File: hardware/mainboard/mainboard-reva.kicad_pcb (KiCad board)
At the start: 4 copper layers, 88 x 48 mm, 77 parts, among them J1 USB-C, J2 BATTERY, J3 SM05B-GHS-TB / ENCODER, J4 SM03B-GHS-TB / SNOOZE, J5 Molex 54550-2472 / GDEY037T03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, J6 Molex 54550-0672 / FL21 front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, J7 SPEAKER, J8 SM02B-GHS-TB / WAKE_LED, Q2 AO3400A / WAKE, U1 ESP32-S3-WROOM-1-N8, U2 BQ24074RGTR, U3 TPS62840DLCR, U4 RV-3028-C7, U5 VEML7700, U6 MAX98357AETE+T, U7 USBLC6-2SC6

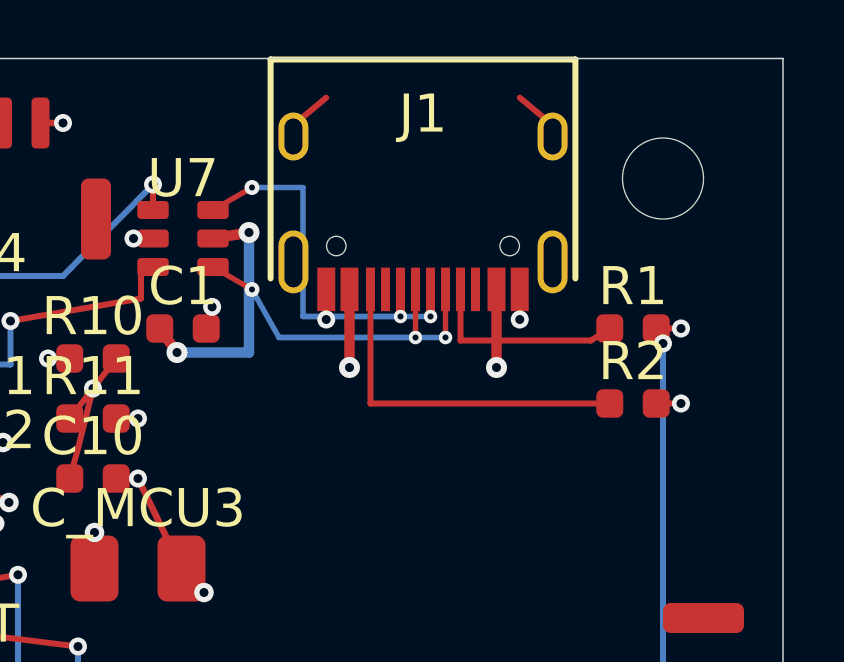
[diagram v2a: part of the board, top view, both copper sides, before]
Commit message: fix(mainboard): rebuild USB-C breakout with rule-compliant geometry
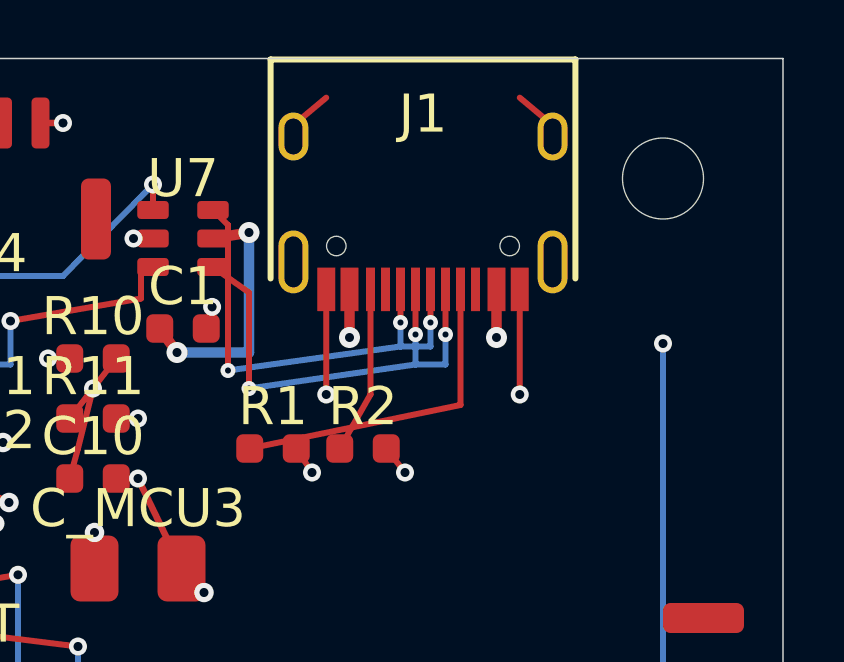
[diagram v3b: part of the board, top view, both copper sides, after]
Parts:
- moved R1 12.6 mm to (71.0, 13.0)
- moved R2 9.12 mm to (74.0, 13.0)
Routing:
- net USB_CC2: track 11.8 -> 5.58 mm
- net GND: track 104.1 -> 109.5 mm
- net USB_CC1: track 6.80 -> 11.0 mm
- net VBUS_USB: track 94.0 -> 91.2 mm
- net USB_D+_CONN: track 16.8 -> 16.2 mm
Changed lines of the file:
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@@
     (pad "" np_thru_hole circle (at -2.89 -2.60) (size 0.65 0.65) (drill 0.65) (layers "*.Cu" "*.Mask"))
     (pad "" np_thru_hole circle (at 2.89 -2.60) (size 0.65 0.65) (drill 0.65) (layers "*.Cu" "*.Mask"))
-    (pad "A1" smd rect (at -3.225 -4.045) (size 0.6 1.45) (layers "F.Cu" "F.Paste" "F.Mask") (net 1 "GND"))
-    (pad "A4" smd rect (at -2.45 -4.045) (size 0.6 1.45) (layers "F.Cu" "F.Paste" "F.Mask") (net 2 "VBUS_USB"))
+    (pad "A1" smd rect (at -3.225 -4.045) (size 0.6 1.45) (layers "F.Cu" "F.Paste" "F.Mask") (clearance 0.15) (net 1 "GND"))
+    (pad "A4" smd rect (at -2.45 -4.045) (size 0.6 1.45) (layers "F.Cu" "F.Paste" "F.Mask") (clearance 0.15) (net 2 "VBUS_USB"))
     (pad "A5" smd rect (at -1.25 -4.045) (size 0.3 1.45) (layers "F.Cu" "F.Paste" "F.Mask") (net 21 "USB_CC1"))
     (pad "A6" smd rect (at -0.25 -4.045) (size 0.3 1.45) (layers "F.Cu" "F.Paste" "F.Mask") (net 59 "USB_D+_CONN"))
     (pad "A7" smd rect (at 0.25 -4.045) (size 0.3 1.45) (layers "F.Cu" "F.Paste" "F.Mask") (net 60 "USB_D-_CONN"))
     (pad "A8" smd rect (at 1.25 -4.045) (size 0.3 1.45) (layers "F.Cu" "F.Paste" "F.Mask"))
-    (pad "A9" smd rect (at 2.45 -4.045) (size 0.6 1.45) (layers "F.Cu" "F.Paste" "F.Mask") (net 2 "VBUS_USB"))
-    (pad "A12" smd rect (at 3.225 -4.045) (size 0.6 1.45) (layers "F.Cu" "F.Paste" "F.Mask") (net 1 "GND"))
+    (pad "A9" smd rect (at 2.45 -4.045) (size 0.6 1.45) (layers "F.Cu" "F.Paste" "F.Mask") (clearance 0.15) (net 2 "VBUS_USB"))
+    (pad "A12" smd rect (at 3.225 -4.045) (size 0.6 1.45) (layers "F.Cu" "F.Paste" "F.Mask") (clearance 0.15) (net 1 "GND"))
     (pad "B5" smd rect (at 1.75 -4.045) (size 0.3 1.45) (layers "F.Cu" "F.Paste" "F.Mask") (net 22 "USB_CC2"))
     (pad "B6" smd rect (at 0.75 -4.045) (size 0.3 1.45) (layers "F.Cu" "F.Paste" "F.Mask") (net 59 "USB_D+_CONN"))
@@
     (pad "6" smd roundrect (at 1 -0.95) (size 1.05 0.6) (layers "F.Cu" "F.Paste" "F.Mask") (roundrect_rratio 0.2) (net 59 "USB_D+_CONN"))
   )
-  (footprint "Resistor_SMD:R_0603_1608Metric" (layer "F.Cu") (at 83.0 9.0)
+  (footprint "Resistor_SMD:R_0603_1608Metric" (layer "F.Cu") (at 71.0 13.0)
     (property "Reference" "R1" (at 0 -1.4) (layer "F.SilkS"))
     (property "Value" "5.1k CC1" (at 0 1.4) (layer "F.Fab") hide)
@@
     (pad "2" smd roundrect (at 0.775 0) (size 0.9 0.95) (layers "F.Cu" "F.Paste" "F.Mask") (roundrect_rratio 0.25) (net 1 "GND"))
   )
-  (footprint "Resistor_SMD:R_0603_1608Metric" (layer "F.Cu") (at 83.0 11.5)
+  (footprint "Resistor_SMD:R_0603_1608Metric" (layer "F.Cu") (at 74.0 13.0)
     (property "Reference" "R2" (at 0 -1.4) (layer "F.SilkS"))
     (property "Value" "5.1k CC2" (at 0 1.4) (layer "F.Fab") hide)
@@
   (via (at 73.0 40.8) (size 0.60) (drill 0.30) (layers "F.Cu" "B.Cu") (net 42))
   (segment (start 73.0 40.8) (end 73.0 42.0) (width 0.30) (layer "F.Cu") (net 42))
-  (segment (start 72.775 7.695) (end 72.775 8.70) (width 0.20) (layer "F.Cu") (net 1))
-  (via (at 72.775 8.70) (size 0.60) (drill 0.30) (layers "F.Cu" "B.Cu") (net 1))
-  (segment (start 79.225 7.695) (end 79.225 8.70) (width 0.20) (layer "F.Cu") (net 1))
-  (via (at 79.225 8.70) (size 0.60) (drill 0.30) (layers "F.Cu" "B.Cu") (net 1))
-  (segment (start 83.775 9.0) (end 84.6 9.0) (width 0.20) (layer "F.Cu") (net 1))
-  (via (at 84.6 9.0) (size 0.60) (drill 0.30) (layers "F.Cu" "B.Cu") (net 1))
-  (segment (start 83.775 11.5) (end 84.6 11.5) (width 0.20) (layer "F.Cu") (net 1))
-  (via (at 84.6 11.5) (size 0.60) (drill 0.30) (layers "F.Cu" "B.Cu") (net 1))
-  (segment (start 77.25 7.695) (end 77.25 9.40) (width 0.20) (layer "F.Cu") (net 21))
-  (segment (start 77.25 9.40) (end 81.60 9.40) (width 0.20) (layer "F.Cu") (net 21))
-  (segment (start 81.60 9.40) (end 82.225 9.00) (width 0.20) (layer "F.Cu") (net 21))
-  (segment (start 74.25 7.695) (end 74.25 11.50) (width 0.20) (layer "F.Cu") (net 22))
-  (segment (start 74.25 11.50) (end 82.225 11.50) (width 0.20) (layer "F.Cu") (net 22))
-  (segment (start 75.25 7.695) (end 75.25 8.60) (width 0.18) (layer "F.Cu") (net 59))
-  (via (at 75.25 8.60) (size 0.45) (drill 0.20) (layers "F.Cu" "B.Cu") (net 59))
-  (segment (start 76.25 7.695) (end 76.25 8.60) (width 0.18) (layer "F.Cu") (net 59))
-  (via (at 76.25 8.60) (size 0.45) (drill 0.20) (layers "F.Cu" "B.Cu") (net 59))
-  (segment (start 75.25 8.60) (end 72.00 8.60) (width 0.18) (layer "B.Cu") (net 59))
-  (segment (start 76.25 8.60) (end 72.00 8.60) (width 0.18) (layer "B.Cu") (net 59))
-  (segment (start 72.00 8.60) (end 72.00 4.30) (width 0.18) (layer "B.Cu") (net 59))
-  (segment (start 72.00 4.30) (end 70.30 4.30) (width 0.18) (layer "B.Cu") (net 59))
-  (via (at 70.30 4.30) (size 0.50) (drill 0.20) (layers "F.Cu" "B.Cu") (net 59))
-  (segment (start 70.30 4.30) (end 69.0 5.05) (width 0.18) (layer "F.Cu") (net 59))
-  (segment (start 75.75 7.695) (end 75.75 9.30) (width 0.18) (layer "F.Cu") (net 60))
-  (via (at 75.75 9.30) (size 0.45) (drill 0.20) (layers "F.Cu" "B.Cu") (net 60))
-  (segment (start 76.75 7.695) (end 76.75 9.30) (width 0.18) (layer "F.Cu") (net 60))
-  (via (at 76.75 9.30) (size 0.45) (drill 0.20) (layers "F.Cu" "B.Cu") (net 60))
-  (segment (start 75.75 9.30) (end 71.20 9.30) (width 0.18) (layer "B.Cu") (net 60))
-  (segment (start 76.75 9.30) (end 71.20 9.30) (width 0.18) (layer "B.Cu") (net 60))
-  (segment (start 71.20 9.30) (end 70.30 7.70) (width 0.18) (layer "B.Cu") (net 60))
-  (via (at 70.30 7.70) (size 0.50) (drill 0.20) (layers "F.Cu" "B.Cu") (net 60))
-  (segment (start 70.30 7.70) (end 69.0 6.95) (width 0.18) (layer "F.Cu") (net 60))
-  (segment (start 73.55 7.695) (end 73.55 10.30) (width 0.35) (layer "F.Cu") (net 2))
-  (via (at 73.55 10.30) (size 0.70) (drill 0.30) (layers "F.Cu" "B.Cu") (net 2))
-  (segment (start 78.45 7.695) (end 78.45 10.30) (width 0.35) (layer "F.Cu") (net 2))
-  (via (at 78.45 10.30) (size 0.70) (drill 0.30) (layers "F.Cu" "B.Cu") (net 2))
-  (segment (start 78.45 10.30) (end 73.55 10.30) (width 0.50) (layer "In2.Cu") (net 2))
-  (segment (start 73.55 10.30) (end 69.80 4.60) (width 0.50) (layer "In2.Cu") (net 2))
+  (segment (start 72.775 7.695) (end 72.775 11.20) (width 0.20) (layer "F.Cu") (net 1))
+  (via (at 72.775 11.20) (size 0.60) (drill 0.30) (layers "F.Cu" "B.Cu") (net 1))
+  (segment (start 79.225 7.695) (end 79.225 11.20) (width 0.20) (layer "F.Cu") (net 1))
+  (via (at 79.225 11.20) (size 0.60) (drill 0.30) (layers "F.Cu" "B.Cu") (net 1))
+  (segment (start 77.25 7.695) (end 77.25 11.55) (width 0.20) (layer "F.Cu") (net 21))
+  (segment (start 77.25 11.55) (end 70.225 13.00) (width 0.20) (layer "F.Cu") (net 21))
+  (segment (start 71.775 13.00) (end 72.30 13.80) (width 0.20) (layer "F.Cu") (net 1))
+  (via (at 72.30 13.80) (size 0.60) (drill 0.30) (layers "F.Cu" "B.Cu") (net 1))
+  (segment (start 74.25 7.695) (end 74.25 11.20) (width 0.20) (layer "F.Cu") (net 22))
+  (segment (start 74.25 11.20) (end 73.225 13.00) (width 0.20) (layer "F.Cu") (net 22))
+  (segment (start 74.775 13.00) (end 75.40 13.80) (width 0.20) (layer "F.Cu") (net 1))
+  (via (at 75.40 13.80) (size 0.60) (drill 0.30) (layers "F.Cu" "B.Cu") (net 1))
+  (segment (start 75.25 7.695) (end 75.25 8.80) (width 0.20) (layer "F.Cu") (net 59))
+  (via (at 75.25 8.80) (size 0.50) (drill 0.20) (layers "F.Cu" "B.Cu") (net 59))
+  (segment (start 76.25 7.695) (end 76.25 8.80) (width 0.20) (layer "F.Cu") (net 59))
+  (via (at 76.25 8.80) (size 0.50) (drill 0.20) (layers "F.Cu" "B.Cu") (net 59))
+  (segment (start 75.25 8.80) (end 75.25 9.60) (width 0.20) (layer "B.Cu") (net 59))
+  (segment (start 76.25 8.80) (end 76.25 9.60) (width 0.20) (layer "B.Cu") (net 59))
+  (segment (start 76.25 9.60) (end 75.25 9.60) (width 0.20) (layer "B.Cu") (net 59))
+  (segment (start 75.25 9.60) (end 69.50 10.40) (width 0.20) (layer "B.Cu") (net 59))
+  (via (at 69.50 10.40) (size 0.50) (drill 0.20) (layers "F.Cu" "B.Cu") (net 59))
+  (segment (start 69.50 10.40) (end 69.50 5.55) (width 0.20) (layer "F.Cu") (net 59))
+  (segment (start 69.50 5.55) (end 69.0 5.05) (width 0.20) (layer "F.Cu") (net 59))
+  (segment (start 75.75 7.695) (end 75.75 9.20) (width 0.20) (layer "F.Cu") (net 60))
+  (via (at 75.75 9.20) (size 0.50) (drill 0.20) (layers "F.Cu" "B.Cu") (net 60))
+  (segment (start 76.75 7.695) (end 76.75 9.20) (width 0.20) (layer "F.Cu") (net 60))
+  (via (at 76.75 9.20) (size 0.50) (drill 0.20) (layers "F.Cu" "B.Cu") (net 60))
+  (segment (start 75.75 9.20) (end 75.75 10.20) (width 0.20) (layer "B.Cu") (net 60))
+  (segment (start 76.75 9.20) (end 76.75 10.20) (width 0.20) (layer "B.Cu") (net 60))
+  (segment (start 76.75 10.20) (end 75.75 10.20) (width 0.20) (layer "B.Cu") (net 60))
+  (segment (start 75.75 10.20) (end 70.20 11.00) (width 0.20) (layer "B.Cu") (net 60))
+  (via (at 70.20 11.00) (size 0.50) (drill 0.20) (layers "F.Cu" "B.Cu") (net 60))
+  (segment (start 70.20 11.00) (end 70.20 7.80) (width 0.20) (layer "F.Cu") (net 60))
+  (segment (start 70.20 7.80) (end 69.0 6.95) (width 0.20) (layer "F.Cu") (net 60))
+  (segment (start 73.55 7.695) (end 73.55 9.30) (width 0.35) (layer "F.Cu") (net 2))
+  (via (at 73.55 9.30) (size 0.70) (drill 0.30) (layers "F.Cu" "B.Cu") (net 2))
+  (segment (start 78.45 7.695) (end 78.45 9.30) (width 0.35) (layer "F.Cu") (net 2))
+  (via (at 78.45 9.30) (size 0.70) (drill 0.30) (layers "F.Cu" "B.Cu") (net 2))
+  (segment (start 78.45 9.30) (end 73.55 9.30) (width 0.50) (layer "In2.Cu") (net 2))
+  (segment (start 73.55 9.30) (end 69.80 4.60) (width 0.50) (layer "In2.Cu") (net 2))
   (segment (start 69.0 6.0) (end 70.20 5.80) (width 0.35) (layer "F.Cu") (net 2))
   (via (at 70.20 5.80) (size 0.70) (drill 0.30) (layers "F.Cu" "B.Cu") (net 2))

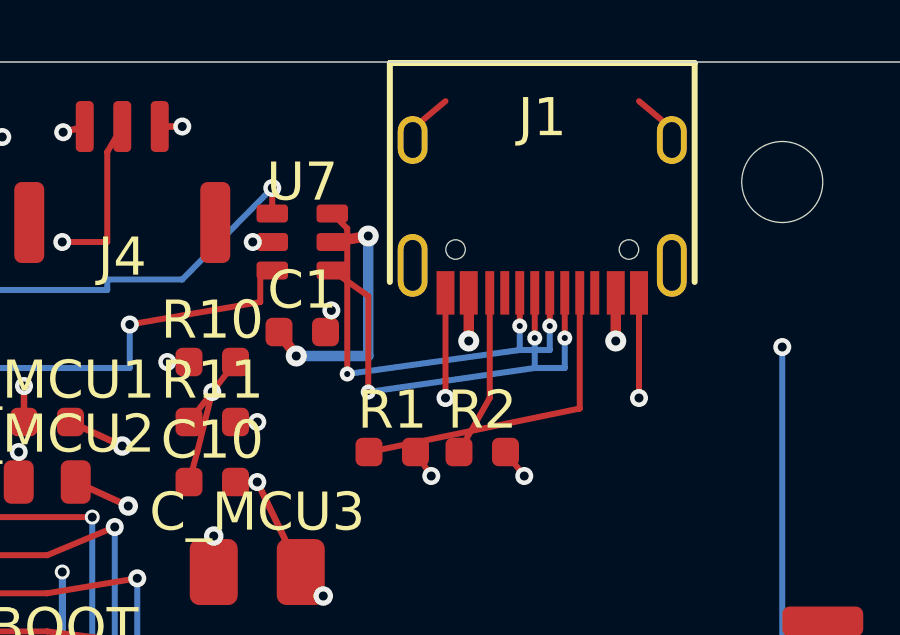
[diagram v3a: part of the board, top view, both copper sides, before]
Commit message: fix(mainboard): separate USB data layers and avoid shell crossing
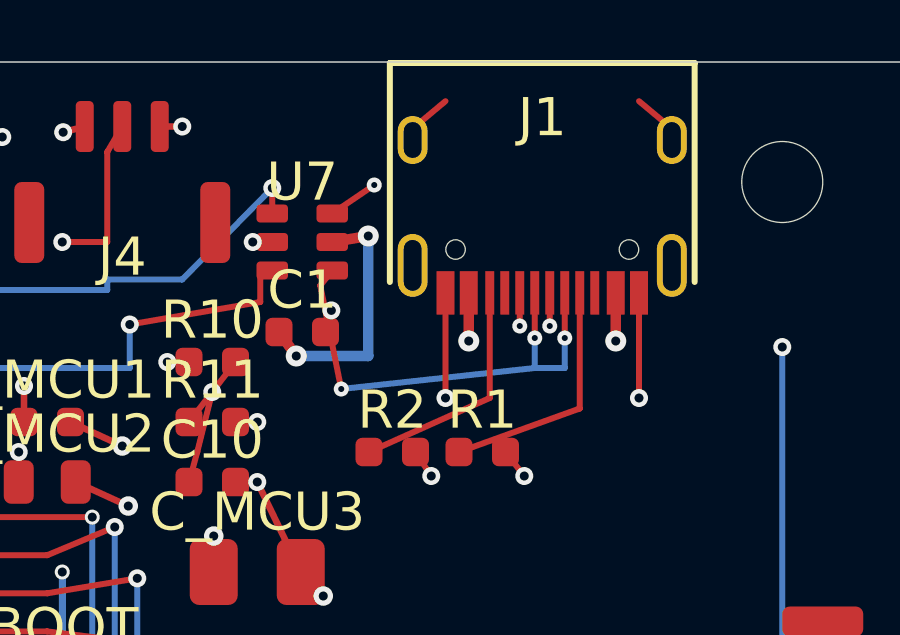
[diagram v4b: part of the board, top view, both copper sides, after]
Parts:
- moved R1 3.00 mm to (74.0, 13.0)
- moved R2 3.00 mm to (71.0, 13.0)
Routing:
- net VBUS_USB: track 91.2 -> 97.4 mm
- net USB_CC1: track 11.0 -> 8.13 mm
- net USB_CC2: track 5.58 -> 7.91 mm
- net USB_D+_CONN: track 16.2 -> 13.8 mm
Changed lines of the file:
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@@
     (pad "6" smd roundrect (at 1 -0.95) (size 1.05 0.6) (layers "F.Cu" "F.Paste" "F.Mask") (roundrect_rratio 0.2) (net 59 "USB_D+_CONN"))
   )
-  (footprint "Resistor_SMD:R_0603_1608Metric" (layer "F.Cu") (at 71.0 13.0)
+  (footprint "Resistor_SMD:R_0603_1608Metric" (layer "F.Cu") (at 74.0 13.0)
     (property "Reference" "R1" (at 0 -1.4) (layer "F.SilkS"))
     (property "Value" "5.1k CC1" (at 0 1.4) (layer "F.Fab") hide)
@@
     (pad "2" smd roundrect (at 0.775 0) (size 0.9 0.95) (layers "F.Cu" "F.Paste" "F.Mask") (roundrect_rratio 0.25) (net 1 "GND"))
   )
-  (footprint "Resistor_SMD:R_0603_1608Metric" (layer "F.Cu") (at 74.0 13.0)
+  (footprint "Resistor_SMD:R_0603_1608Metric" (layer "F.Cu") (at 71.0 13.0)
     (property "Reference" "R2" (at 0 -1.4) (layer "F.SilkS"))
     (property "Value" "5.1k CC2" (at 0 1.4) (layer "F.Fab") hide)
@@
   (via (at 79.225 11.20) (size 0.60) (drill 0.30) (layers "F.Cu" "B.Cu") (net 1))
   (segment (start 77.25 7.695) (end 77.25 11.55) (width 0.20) (layer "F.Cu") (net 21))
-  (segment (start 77.25 11.55) (end 70.225 13.00) (width 0.20) (layer "F.Cu") (net 21))
+  (segment (start 77.25 11.55) (end 73.225 13.00) (width 0.20) (layer "F.Cu") (net 21))
   (segment (start 71.775 13.00) (end 72.30 13.80) (width 0.20) (layer "F.Cu") (net 1))
   (via (at 72.30 13.80) (size 0.60) (drill 0.30) (layers "F.Cu" "B.Cu") (net 1))
   (segment (start 74.25 7.695) (end 74.25 11.20) (width 0.20) (layer "F.Cu") (net 22))
-  (segment (start 74.25 11.20) (end 73.225 13.00) (width 0.20) (layer "F.Cu") (net 22))
+  (segment (start 74.25 11.20) (end 70.225 13.00) (width 0.20) (layer "F.Cu") (net 22))
   (segment (start 74.775 13.00) (end 75.40 13.80) (width 0.20) (layer "F.Cu") (net 1))
   (via (at 75.40 13.80) (size 0.60) (drill 0.30) (layers "F.Cu" "B.Cu") (net 1))
@@
   (segment (start 76.25 7.695) (end 76.25 8.80) (width 0.20) (layer "F.Cu") (net 59))
   (via (at 76.25 8.80) (size 0.50) (drill 0.20) (layers "F.Cu" "B.Cu") (net 59))
-  (segment (start 75.25 8.80) (end 75.25 9.60) (width 0.20) (layer "B.Cu") (net 59))
-  (segment (start 76.25 8.80) (end 76.25 9.60) (width 0.20) (layer "B.Cu") (net 59))
-  (segment (start 76.25 9.60) (end 75.25 9.60) (width 0.20) (layer "B.Cu") (net 59))
-  (segment (start 75.25 9.60) (end 69.50 10.40) (width 0.20) (layer "B.Cu") (net 59))
-  (via (at 69.50 10.40) (size 0.50) (drill 0.20) (layers "F.Cu" "B.Cu") (net 59))
-  (segment (start 69.50 10.40) (end 69.50 5.55) (width 0.20) (layer "F.Cu") (net 59))
-  (segment (start 69.50 5.55) (end 69.0 5.05) (width 0.20) (layer "F.Cu") (net 59))
+  (segment (start 75.25 8.80) (end 75.25 9.60) (width 0.20) (layer "In1.Cu") (net 59))
+  (segment (start 76.25 8.80) (end 76.25 9.60) (width 0.20) (layer "In1.Cu") (net 59))
+  (segment (start 76.25 9.60) (end 75.25 9.60) (width 0.20) (layer "In1.Cu") (net 59))
+  (segment (start 75.25 9.60) (end 70.40 4.10) (width 0.20) (layer "In1.Cu") (net 59))
+  (via (at 70.40 4.10) (size 0.50) (drill 0.20) (layers "F.Cu" "B.Cu") (net 59))
+  (segment (start 70.40 4.10) (end 69.0 5.05) (width 0.20) (layer "F.Cu") (net 59))
   (segment (start 75.75 7.695) (end 75.75 9.20) (width 0.20) (layer "F.Cu") (net 60))
   (via (at 75.75 9.20) (size 0.50) (drill 0.20) (layers "F.Cu" "B.Cu") (net 60))
@@
   (segment (start 76.75 9.20) (end 76.75 10.20) (width 0.20) (layer "B.Cu") (net 60))
   (segment (start 76.75 10.20) (end 75.75 10.20) (width 0.20) (layer "B.Cu") (net 60))
-  (segment (start 75.75 10.20) (end 70.20 11.00) (width 0.20) (layer "B.Cu") (net 60))
-  (via (at 70.20 11.00) (size 0.50) (drill 0.20) (layers "F.Cu" "B.Cu") (net 60))
-  (segment (start 70.20 11.00) (end 70.20 7.80) (width 0.20) (layer "F.Cu") (net 60))
-  (segment (start 70.20 7.80) (end 69.0 6.95) (width 0.20) (layer "F.Cu") (net 60))
+  (segment (start 75.75 10.20) (end 69.30 10.90) (width 0.20) (layer "B.Cu") (net 60))
+  (via (at 69.30 10.90) (size 0.50) (drill 0.20) (layers "F.Cu" "B.Cu") (net 60))
+  (segment (start 69.30 10.90) (end 68.60 7.45) (width 0.20) (layer "F.Cu") (net 60))
+  (segment (start 68.60 7.45) (end 69.0 6.95) (width 0.20) (layer "F.Cu") (net 60))
   (segment (start 73.55 7.695) (end 73.55 9.30) (width 0.35) (layer "F.Cu") (net 2))
   (via (at 73.55 9.30) (size 0.70) (drill 0.30) (layers "F.Cu" "B.Cu") (net 2))
@@
   (via (at 78.45 9.30) (size 0.70) (drill 0.30) (layers "F.Cu" "B.Cu") (net 2))
   (segment (start 78.45 9.30) (end 73.55 9.30) (width 0.50) (layer "In2.Cu") (net 2))
-  (segment (start 73.55 9.30) (end 69.80 4.60) (width 0.50) (layer "In2.Cu") (net 2))
+  (segment (start 73.55 9.30) (end 73.55 11.20) (width 0.50) (layer "In2.Cu") (net 2))
+  (segment (start 73.55 11.20) (end 69.80 11.20) (width 0.50) (layer "In2.Cu") (net 2))
+  (segment (start 69.80 11.20) (end 69.80 4.60) (width 0.50) (layer "In2.Cu") (net 2))
   (segment (start 69.0 6.0) (end 70.20 5.80) (width 0.35) (layer "F.Cu") (net 2))
   (via (at 70.20 5.80) (size 0.70) (drill 0.30) (layers "F.Cu" "B.Cu") (net 2))
